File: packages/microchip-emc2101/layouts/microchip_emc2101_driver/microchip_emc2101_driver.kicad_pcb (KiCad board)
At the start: 2 copper layers, 6 parts

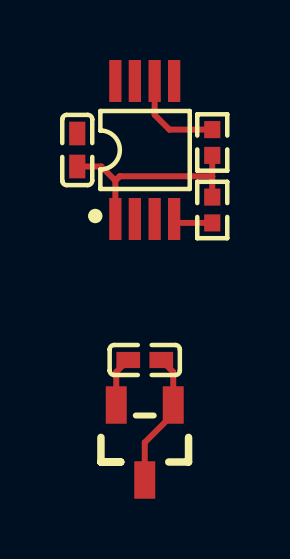
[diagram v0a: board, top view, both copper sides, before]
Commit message: Manually fix fp lib tables
fix some small bugs
fix package only modules (e.g. logos)
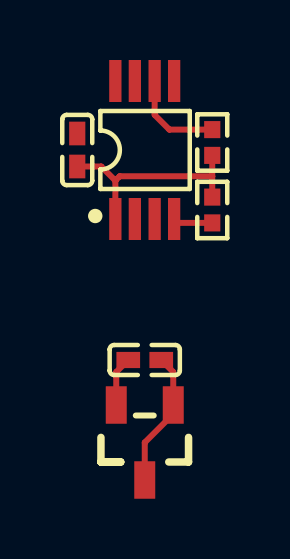
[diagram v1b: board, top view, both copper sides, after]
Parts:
- C1: footprint atopile:C0402-b3ef17 -> Samsung_Electro_Mechanics_CL05B104KO5NNNC:C0402
- C2: footprint atopile:C0402-b3ef17 -> FH_0402B222K500NT:C0402
- Q1: footprint atopile:SOT-23-3_L2.9-W1.3-P1.90-LS2.4-TR-36f2d9 -> KEC_Semicon_2N3906S_RTK_PS:SOT-23-3_L2.9-W1.3-P1.90-LS2.4-TR
- R1, R2: footprint atopile:R0402-56259e -> UNI_ROYAL_0402WGF1002TCE:R0402
- U1: footprint atopile:MSOP-8_L3.0-W3.0-P0.65-LS4.9-BL-3bf91a -> Microchip_Tech_EMC2101_R_ACZL_TR:MSOP-8_L3.0-W3.0-P0.65-LS4.9-BL

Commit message: Update 3D model locations
fix missing renders
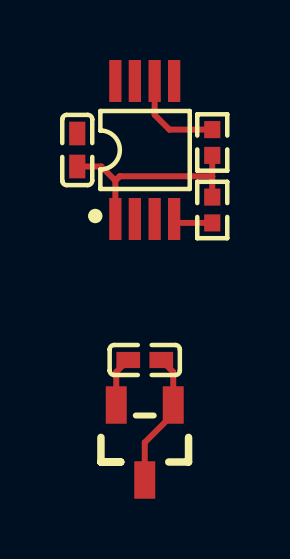
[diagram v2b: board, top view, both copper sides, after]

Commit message: rebuild all packages & regenerate images of changed layouts (silk)
Add new scripts for version bump and build (based on atopile/packages)
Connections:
- net base renamed DN
- net emitter renamed DP

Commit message: Use packages from packages folder
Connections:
- net ALERTh_TACH renamed nALERT_TACH
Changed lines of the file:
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@@
     (net 1 "SMDATA")
     (net 2 "SMCLK")
-    (net 3 "ALERTh_TACH")
+    (net 3 "nALERT_TACH")
     (net 4 "gnd")
     (net 5 "FAN")
@@
             (size 0.41 1.4)
             (layers "F.Cu" "F.Mask" "F.Paste")
-            (net 3 "ALERTh_TACH")
+            (net 3 "nALERT_TACH")
         )
         (pad "7" smd rect
@@
             (size 0.57 0.54)
             (layers "F.Cu" "F.Mask" "F.Paste")
-            (net 3 "ALERTh_TACH")
+            (net 3 "nALERT_TACH")
         )
         (pad "2" smd rect
